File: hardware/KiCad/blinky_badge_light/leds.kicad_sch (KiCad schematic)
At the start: 48 parts

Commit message: updates to hardware schematic
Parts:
- added C36, C37: 100nF, Capacitor_SMD:C_0402_1005Metric, symbol Device:C
- added U6: SN74LVC1T45DBV, Package_TO_SOT_SMD:SOT-23-6, symbol Logic_LevelTranslator:SN74LVC1T45DBV
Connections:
- net 5V Power: now also C37.2, U6.1 (VCCA)
- net GND: now also C36.1, C37.1, U6.2 (GND), U6.5 (DIR)
- net LED DATA: now also U6.4 (B); no longer D1.4 (DIN)
- new net 3.3V Power: C36.2, U6.6 (VCCB)
- new net SHIFTED LED DATA: D1.4 (DIN), U6.3 (A)
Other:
- note added: "LEVEL SHIFTER"
- moved on the sheet: D1, D10, D11, D12, D13, D14, D15, D16, D17, D18, D19, D2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

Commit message: placing items on the board
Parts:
- added C: 100nF, Capacitor_SMD:C_0402_1005Metric, symbol Device:C
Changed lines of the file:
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@@
+	)
+	(symbol
+		(lib_id "Device:C")
+		(at 228.6 49.53 90)
+		(unit 1)
+		(exclude_from_sim no)
+		(in_bom yes)
+		(on_board yes)
+		(dnp no)
+		(fields_autoplaced yes)
+		(property "Reference" "C"
+			(at 228.6 41.91 90)
+			(effects
+				(font
+					(size 1.27 1.27)
+				)
+			)
+		)
+		(property "Value" "100nF"
+			(at 228.6 44.45 90)
+			(effects
+				(font
+					(size 1.27 1.27)
+				)
+			)
+		)
+		(property "Footprint" "Capacitor_SMD:C_0402_1005Metric"
+			(at 232.41 48.5648 0)
+			(effects
+				(font
+					(size 1.27 1.27)
+				)
+				(hide yes)
+			)
+		)
+		(property "Datasheet" "https://www.lcsc.com/datasheet/lcsc_datasheet_2304140030_Samsung-Electro-Mechanics-CL05B104KO5NNNC_C1525.pdf"
+			(at 228.6 49.53 0)
+			(effects
+				(font
+					(size 1.27 1.27)
+				)
+				(hide yes)
+			)
+		)
+		(property "Description" "Unpolarized capacitor"
+			(at 228.6 49.53 0)
+			(effects
+				(font
+					(size 1.27 1.27)
+				)
+				(hide yes)
+			)
+		)
+		(property "JLCPCB Part #" "C1525"
+			(at 228.6 49.53 0)
+			(effects
+				(font
+					(size 1.27 1.27)
+				)
+				(hide yes)
+			)
+		)
+		(pin "1"
+		)
+		(pin "2"
+		)
+		(instances
+			(project "blinky_badge_light"
+				(path "/f33039b1-b38b-4cb6-baf0-07a137773378/a31a264e-f1c4-410a-a175-a81c007586a2"
+					(reference "C29")
+					(unit 1)
+				)
+			)
+		)
 	)
 	(symbol

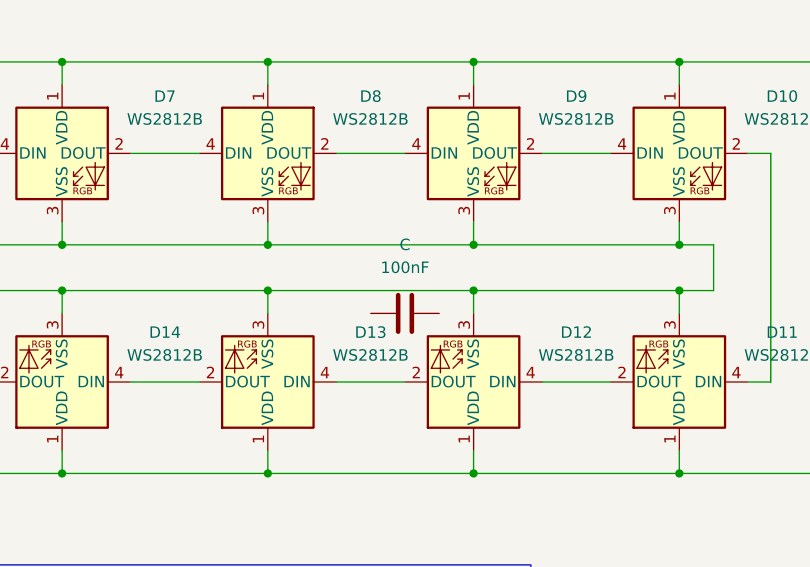
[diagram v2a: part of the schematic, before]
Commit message: fix some stuff with the footprints, rearrange some things
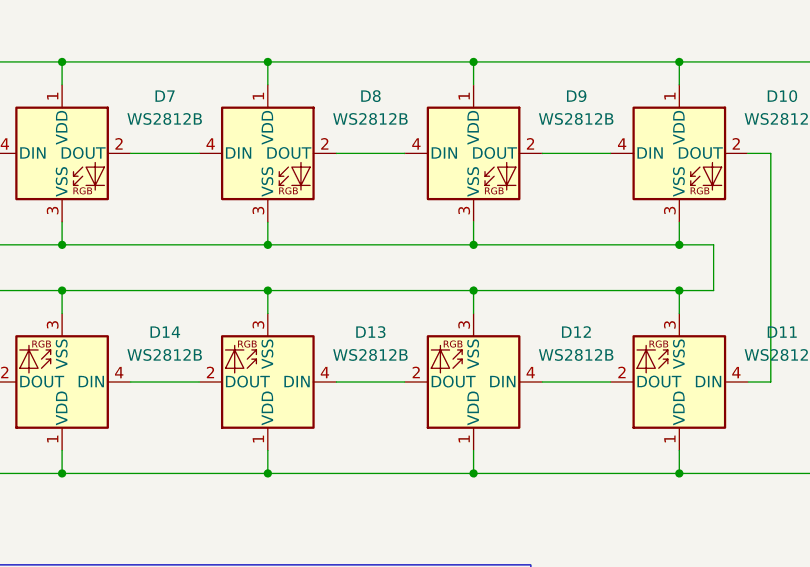
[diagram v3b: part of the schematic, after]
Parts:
- removed C: 100nF, Capacitor_SMD:C_0402_1005Metric, symbol Device:C
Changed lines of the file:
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@@
-	)
-	(symbol
-		(lib_id "Device:C")
-		(at 228.6 49.53 90)
-		(unit 1)
-		(exclude_from_sim no)
-		(in_bom yes)
-		(on_board yes)
-		(dnp no)
-		(fields_autoplaced yes)
-		(property "Reference" "C"
-			(at 228.6 41.91 90)
-			(effects
-				(font
-					(size 1.27 1.27)
-				)
-			)
-		)
-		(property "Value" "100nF"
-			(at 228.6 44.45 90)
-			(effects
-				(font
-					(size 1.27 1.27)
-				)
-			)
-		)
-		(property "Footprint" "Capacitor_SMD:C_0402_1005Metric"
-			(at 232.41 48.5648 0)
-			(effects
-				(font
-					(size 1.27 1.27)
-				)
-				(hide yes)
-			)
-		)
-		(property "Datasheet" "https://www.lcsc.com/datasheet/lcsc_datasheet_2304140030_Samsung-Electro-Mechanics-CL05B104KO5NNNC_C1525.pdf"
-			(at 228.6 49.53 0)
-			(effects
-				(font
-					(size 1.27 1.27)
-				)
-				(hide yes)
-			)
-		)
-		(property "Description" "Unpolarized capacitor"
-			(at 228.6 49.53 0)
-			(effects
-				(font
-					(size 1.27 1.27)
-				)
-				(hide yes)
-			)
-		)
-		(property "JLCPCB Part #" "C1525"
-			(at 228.6 49.53 0)
-			(effects
-				(font
-					(size 1.27 1.27)
-				)
-				(hide yes)
-			)
-		)
-		(pin "1"
-		)
-		(pin "2"
-		)
-		(instances
-			(project "blinky_badge_light"
-				(path "/f33039b1-b38b-4cb6-baf0-07a137773378/a31a264e-f1c4-410a-a175-a81c007586a2"
-					(reference "C29")
-					(unit 1)
-				)
-			)
-		)
 	)
 	(symbol
